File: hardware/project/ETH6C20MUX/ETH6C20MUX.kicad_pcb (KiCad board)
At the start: 4 copper layers, 160 x 100 mm, 184 parts, among them J301 5499141-4, J501 Conn_01x06, J502 Conn_02x08_Odd_Even, J503 C64AC, J601 Conn_02x05, J602 Conn_02x01, K301 HE3621A0510, K302 HE3621A0510, K303 HE3621A0510, K304 HE3621A0510, K305 HE3621A0510, K306 HE3621A0510, K307 HE3621A0510, K308 HE3621A0510, K309 HE3621A0510, K310 HE3621A0510, K311 HE3621A0510, K312 HE3621A0510, K313 HE3621A0510, K314 HE3621A0510, K315 HE3621A0510, K316 HE3621A0510, K317 HE3621A0510, K318 HE3621A0510, K319 HE3621A0510, K320 HE3621A0510, K321 HE3621A0510, K322 HE3621A0510, K323 HE3621A0510, K324 HE3621A0510, K325 HE3621A0510, K326 HE3621A0510, K327 HE3621A0510, K328 HE3621A0510, K329 HE3621A0510, K330 HE3621A0510, K331 HE3621A0510, K332 HE3621A0510, K333 HE3621A0510, K334 HE3621A0510, K335 HE3621A0510, K336 HE3621A0510, K337 HE3621A0510, K338 HE3621A0510, K339 HE3621A0510, K340 HE3621A0510, K341 HE3621A0510, K342 HE3621A0510, K343 HE3621A0510, K344 HE3621A0510, K345 HE3621A0510, K346 HE3621A0510, K347 HE3621A0510, K348 HE3621A0510, K349 HE3621A0510, K350 HE3621A0510, K351 HE3621A0510, K352 HE3621A0510, K353 HE3621A0510, K354 HE3621A0510, K355 HE3621A0510, K356 HE3621A0510, K357 HE3621A0510, K358 HE3621A0510, K359 HE3621A0510, K360 HE3621A0510, K361 HE3621A0510, K362 HE3621A0510, K363 HE3621A0510, K364 HE3621A0510, K365 HE3621A0510, K366 HE3621A0510, Q401 IRFR5410, U201 LC03-3.3, U202 LAN8742A, U203 LC03-3.3, U301 MCZ33996, U302 MCZ33996, U303 MCZ33996, U304 MCZ33996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

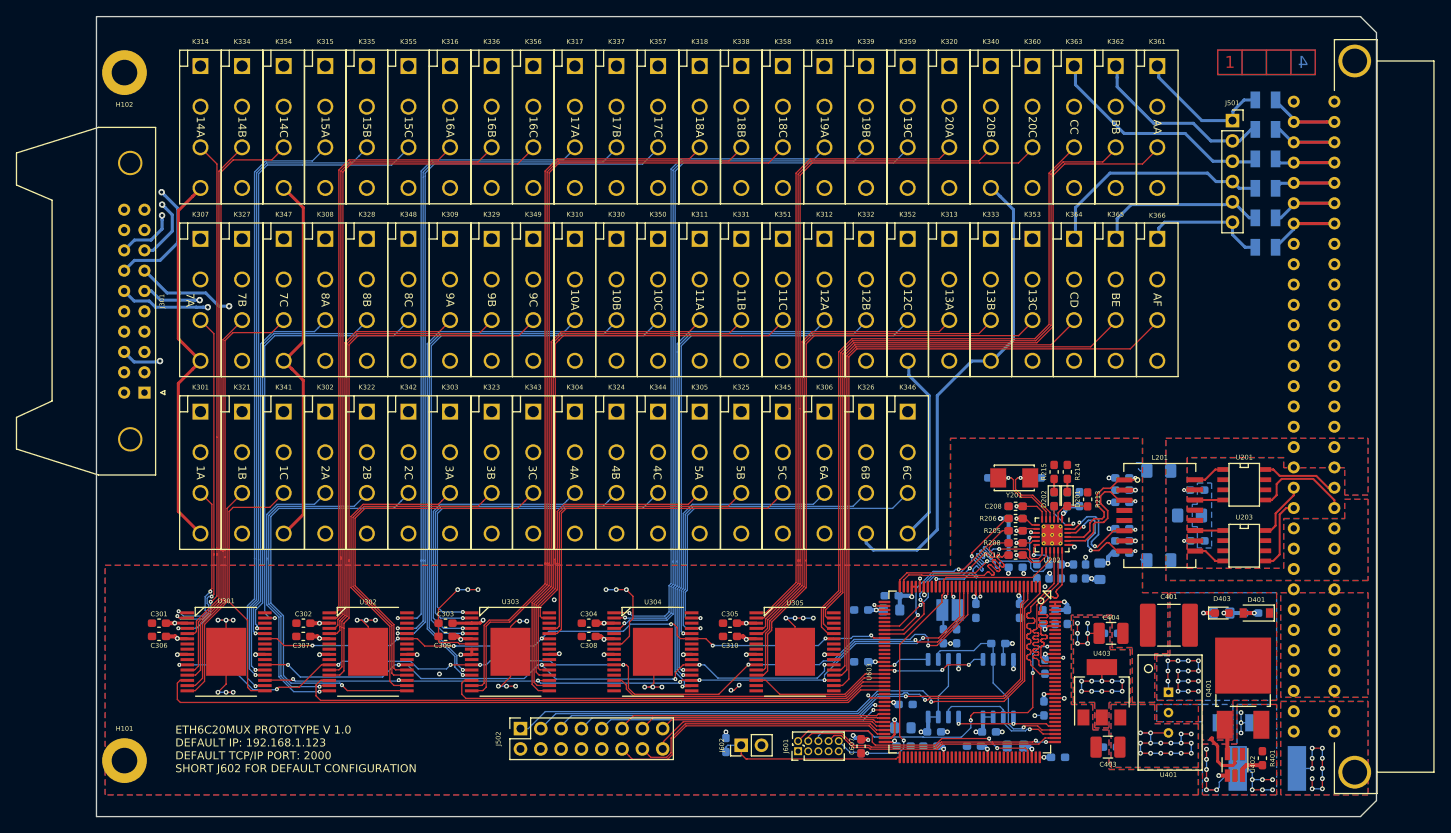
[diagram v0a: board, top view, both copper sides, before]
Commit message: SPI6C20MUX layout done, bug fixes in ETH6C20MUX layout.
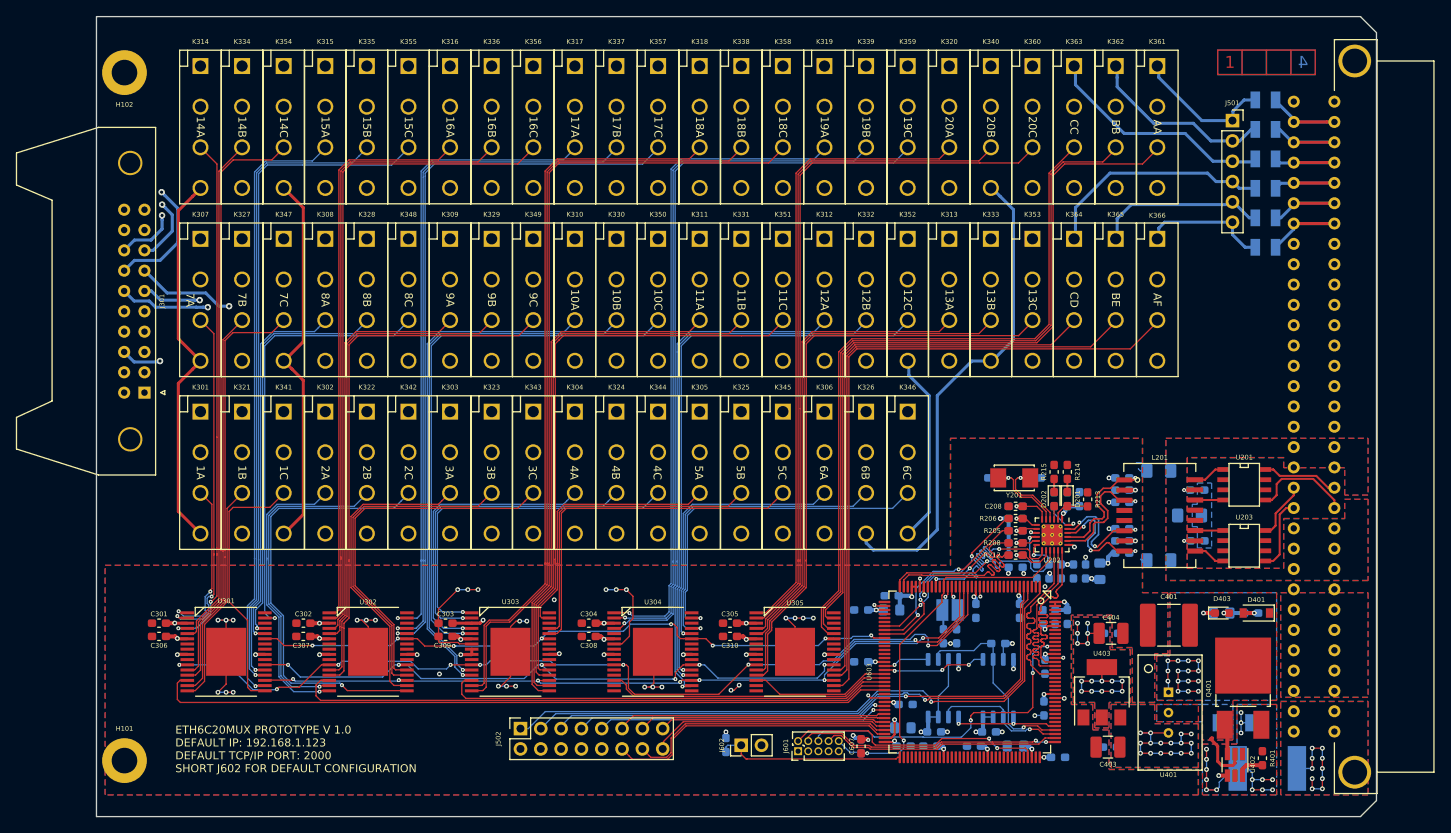
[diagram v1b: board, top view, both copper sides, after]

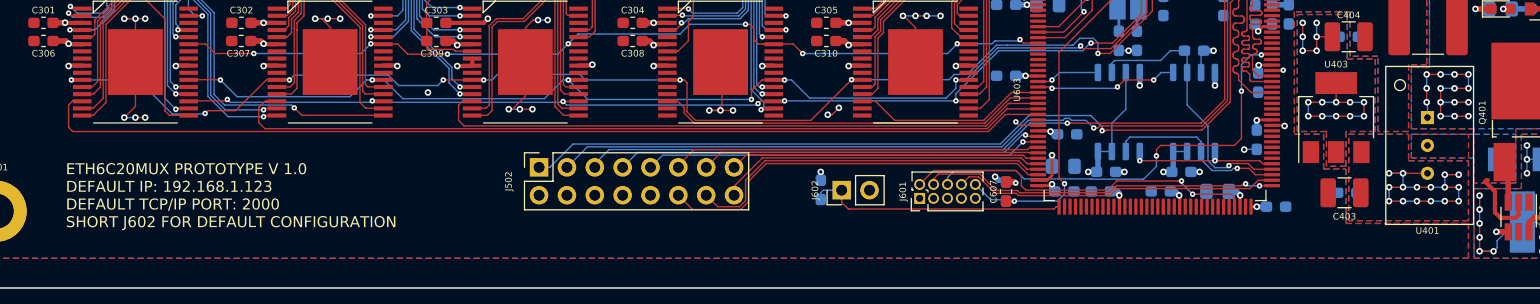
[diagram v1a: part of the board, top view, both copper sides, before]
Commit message: Bug fix in TSR2 2450 footprint.
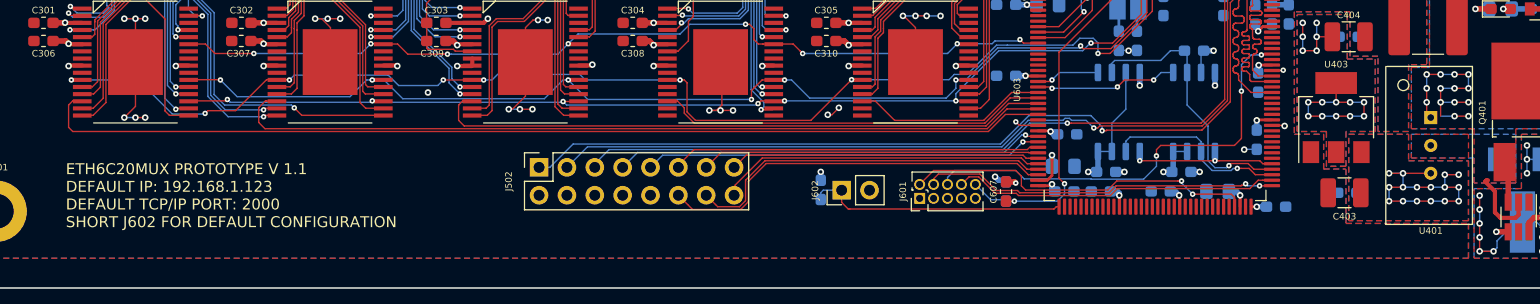
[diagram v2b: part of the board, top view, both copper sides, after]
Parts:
- moved U401 0.30 mm to (194.3, 127.0)
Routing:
- net Net-(C401-Pad1): track 26.3 -> 26.5 mm, vias 15 -> 14
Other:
- board text added: "ETH6C20MUX PROTOTYPE V 1.1 DEFAULT IP: 192.168.1.123 DEFAULT TCP/IP PORT: 2000 SHORT J602 FOR DEFAULT CONFIGURATION"
- board text removed: "ETH6C20MUX PROTOTYPE V 1.0 DEFAULT IP: 192.168.1.123 DEFAULT TCP/IP PORT: 2000 SHORT J602 FOR DEFAULT CONFIGURATION"
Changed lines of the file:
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@@
   )
   (setup
-    (last_trace_width 0.381)
+    (last_trace_width 0.127)
     (user_trace_width 0.254)
     (user_trace_width 0.381)
@@
     (add_net /Relays/PIN9)
   )
+  (module ETH6C20MUX:TSR2 (layer Top)
+    (at 194.3 127 270)
+    (descr "DC/DC Converter TSR 2 Series, 2 A")
+    (fp_text reference U401 (at 7.779 0 180) (layer F.SilkS)
+      (effects (font (size 0.6 0.6) (thickness 0.12)))
+    )
+    (fp_text value TSR2-2450 (at 0 1.778 90) (layer F.Fab)
+      (effects (font (size 1 1) (thickness 0.15)))
+    )
+    (fp_circle (center -5.5 2.5) (end -5.5 3) (layer F.SilkS) (width 0.12))
+    (fp_line (start 7.3 4.2) (end -7.3 4.2) (layer F.CrtYd) (width 0.12))
+    (fp_line (start -7.3 4.2) (end -7.3 -3.9) (layer F.CrtYd) (width 0.12))
+    (fp_line (start 7.3 -3.9) (end 7.3 4.2) (layer F.CrtYd) (width 0.12))
+    (fp_line (start -7.3 -3.9) (end 7.3 -3.9) (layer F.CrtYd) (width 0.12))
+    (fp_line (start -7.2 -3.8) (end 7.2 -3.8) (layer F.SilkS) (width 0.12))
+    (fp_line (start -7.2 4) (end -7.2 -3.8) (layer F.SilkS) (width 0.12))
+    (fp_line (start 7.2 4.1) (end -7.2 4.1) (layer F.SilkS) (width 0.12))
+    (fp_line (start 7.2 -3.8) (end 7.2 4.1) (layer F.SilkS) (width 0.12))
+    (pad 3 thru_hole circle (at 2.54 0 270) (size 1.2 1.2) (drill 0.6) (layers *.Cu *.Mask)
+      (net 8 +5V))
+    (pad 2 thru_hole circle (at 0 0 270) (size 1.2 1.2) (drill 0.6) (layers *.Cu *.Mask)
+      (net 1 GND))
+    (pad 1 thru_hole rect (at -2.54 0 270) (size 1.2 1.2) (drill 0.6) (layers *.Cu *.Mask)
+      (net 7 "Net-(C401-Pad1)"))
+    (model ${ETH6C20MUX}/tsr2.STEP
+      (offset (xyz 0 0.15 10.05))
+      (scale (xyz 1 1 1))
+      (rotate (xyz 180 0 0))
+    )
+  )
   (module ETH6C20MUX:NX5032GA (layer Top)
     (at 174.72 97.663 180)
@@
     )
   )
-  (module ETH6C20MUX:TSR2 (layer Top)
-    (at 194 127 270)
-    (descr "DC/DC Converter TSR 2 Series, 2 A")
-    (fp_text reference U401 (at 7.779 0 180) (layer F.SilkS)
-      (effects (font (size 0.6 0.6) (thickness 0.12)))
-    )
-    (fp_text value TSR2-2450 (at 0 1.778 90) (layer F.Fab)
-      (effects (font (size 1 1) (thickness 0.15)))
-    )
-    (fp_circle (center -5.5 2.5) (end -5.5 3) (layer F.SilkS) (width 0.12))
-    (fp_line (start 7.3 3.9) (end -7.3 3.9) (layer F.CrtYd) (width 0.12))
-    (fp_line (start -7.3 3.9) (end -7.3 -4.3) (layer F.CrtYd) (width 0.12))
-    (fp_line (start 7.3 -4.3) (end 7.3 3.9) (layer F.CrtYd) (width 0.12))
-    (fp_line (start -7.3 -4.3) (end 7.3 -4.3) (layer F.CrtYd) (width 0.12))
-    (fp_line (start -7.2 -4.2) (end 7.2 -4.2) (layer F.SilkS) (width 0.12))
-    (fp_line (start -7.2 3.8) (end -7.2 -4.2) (layer F.SilkS) (width 0.12))
-    (fp_line (start 7.2 3.8) (end -7.2 3.8) (layer F.SilkS) (width 0.12))
-    (fp_line (start 7.2 -4.2) (end 7.2 3.8) (layer F.SilkS) (width 0.12))
-    (pad 3 thru_hole circle (at 2.54 0 270) (size 1.2 1.2) (drill 0.6) (layers *.Cu *.Mask)
-      (net 8 +5V))
-    (pad 2 thru_hole circle (at 0 0 270) (size 1.2 1.2) (drill 0.6) (layers *.Cu *.Mask)
-      (net 1 GND))
-    (pad 1 thru_hole rect (at -2.54 0 270) (size 1.2 1.2) (drill 0.6) (layers *.Cu *.Mask)
-      (net 7 "Net-(C401-Pad1)"))
-    (model ${ETH6C20MUX}/tsr2.STEP
-      (offset (xyz 0 0.15 10.05))
-      (scale (xyz 1 1 1))
-      (rotate (xyz 180 0 0))
-    )
-  )
   (module ETH6C20MUX:HE360_x-5331272-5 (layer Top)
     (at 99 53.8 270)
@@
   (gr_line (start 208.534 125.73) (end 210.566 125.73) (layer B.SilkS) (width 0.15))
   (gr_line (start 210.566 130.429) (end 208.534 130.429) (layer B.SilkS) (width 0.15))
-  (gr_text "ETH6C20MUX PROTOTYPE V 1.0\nDEFAULT IP: 192.168.1.123\nDEFAULT TCP/IP PORT: 2000\nSHORT J602 FOR DEFAULT CONFIGURATION" (at 69.85 131.572) (layer F.SilkS)
+  (gr_text "ETH6C20MUX PROTOTYPE V 1.1\nDEFAULT IP: 192.168.1.123\nDEFAULT TCP/IP PORT: 2000\nSHORT J602 FOR DEFAULT CONFIGURATION" (at 69.85 131.572) (layer F.SilkS)
     (effects (font (size 1 1) (thickness 0.15)) (justify left))
   )
@@
   (segment (start 161.914 111.2575) (end 161.914 112.511) (width 0.254) (layer Top) (net 6))
   (via (at 193.929 123.063) (size 0.6) (drill 0.3) (layers Top Bottom) (net 7))
-  (segment (start 194 124.46) (end 194 123.134) (width 0.127) (layer Bottom) (net 7))
   (segment (start 194 123.134) (end 193.929 123.063) (width 0.127) (layer Bottom) (net 7))
   (via (at 193.929 121.793) (size 0.6) (drill 0.3) (layers Top Bottom) (net 7))
@@
   (via (at 197.739 123.063) (size 0.6) (drill 0.3) (layers Top Bottom) (net 7))
   (segment (start 196.469 123.063) (end 197.739 123.063) (width 0.127) (layer Top) (net 7))
-  (via (at 195.199 124.333) (size 0.6) (drill 0.3) (layers Top Bottom) (net 7))
   (segment (start 195.199 123.063) (end 195.199 124.333) (width 0.127) (layer Top) (net 7))
   (via (at 196.469 124.333) (size 0.6) (drill 0.3) (layers Top Bottom) (net 7))
@@
   (segment (start 200.66 133.604) (end 200.152 133.096) (width 0.381) (layer Top) (net 7))
   (segment (start 200.152 133.096) (end 200.152 131.191) (width 0.381) (layer Top) (net 7))
+  (segment (start 193.929 124.079) (end 194.31 124.46) (width 0.127) (layer Top) (net 7))
+  (segment (start 193.929 123.063) (end 193.929 124.079) (width 0.127) (layer Top) (net 7))
   (via (at 70.104 117.729) (size 0.6) (drill 0.3) (layers Top Bottom) (net 8))
   (segment (start 70.13 117.755) (end 70.104 117.729) (width 0.381) (layer Top) (net 8))
